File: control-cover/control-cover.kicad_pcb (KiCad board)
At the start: 2 copper layers, 60 x 35 mm, 9 parts

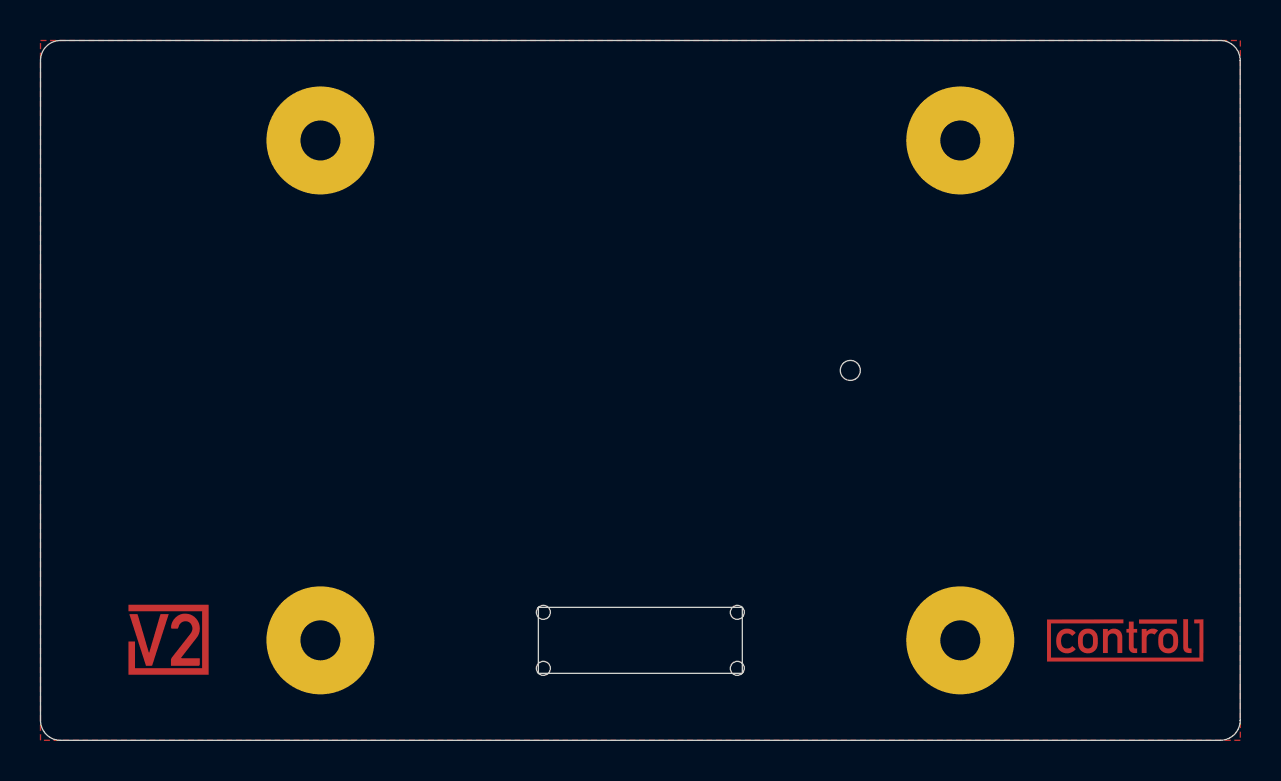
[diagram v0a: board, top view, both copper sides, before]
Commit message: Replace Order_Number
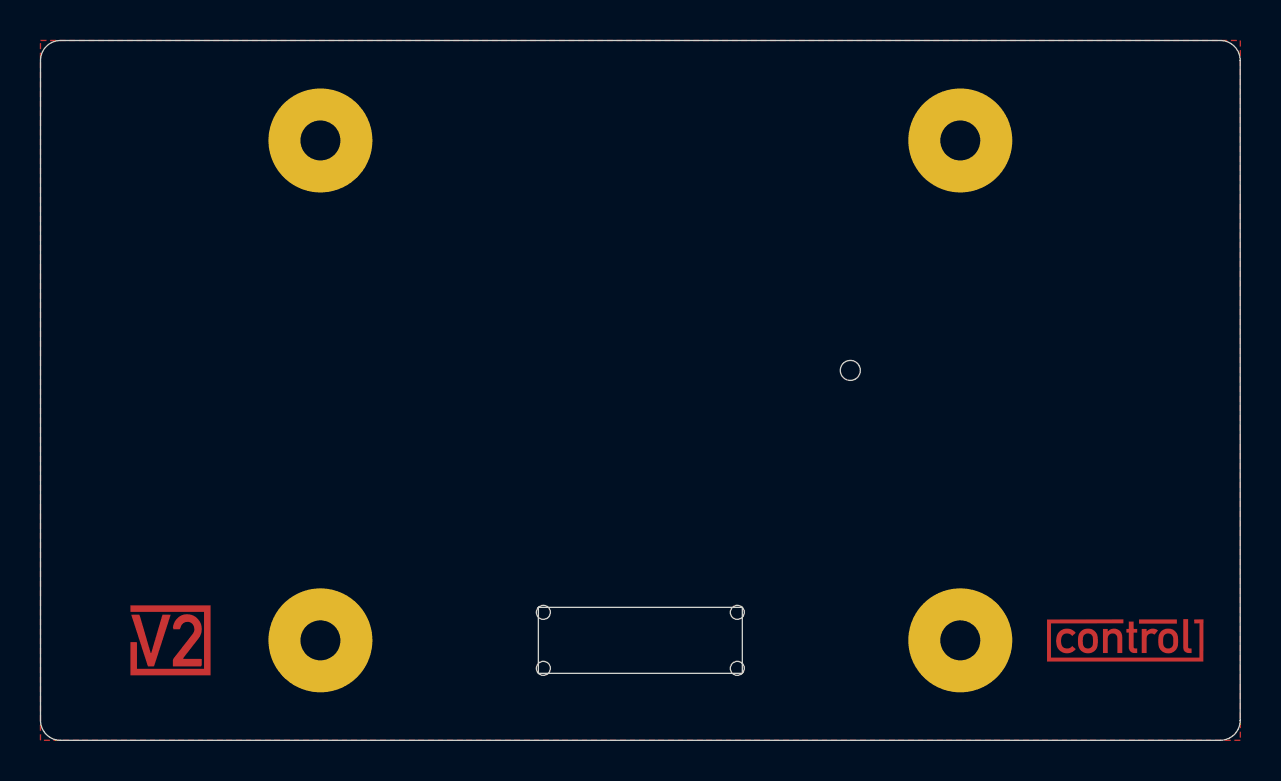
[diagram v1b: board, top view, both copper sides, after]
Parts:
- H101, H102, H103, H104: value MountingHole_2mm_Pad_5.2mm -> 2mm_Pad_5.2mm; footprint V2_Mechanical:Mounting_Hole_2mm_Pad_5.2mm -> V2_Mechanical:MountingHole_2mm_Pad_5.2mm
- H105: value MountingHole_1mm -> 1mm
- INFO101: value ORDER-NUMBER -> ~; footprint V2_Production:Order_Number -> V2_Production:Revision
